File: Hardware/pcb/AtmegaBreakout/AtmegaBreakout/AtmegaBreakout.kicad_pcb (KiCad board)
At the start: 4 copper layers, 69.9 x 53.3 mm, 33 parts, among them J1 ANALOG, J2 POWER and COMMS, J3 DIGITAL1, J4 DIGITAL2, J5 DIGITAL3, J6 USB_B_Micro, SW1 EVP-ASAC1A, U1 ATMEGA2560-16AU, U2 CP2102N-A01-GQFN24, Y1 16MHz Ceramic Resonator

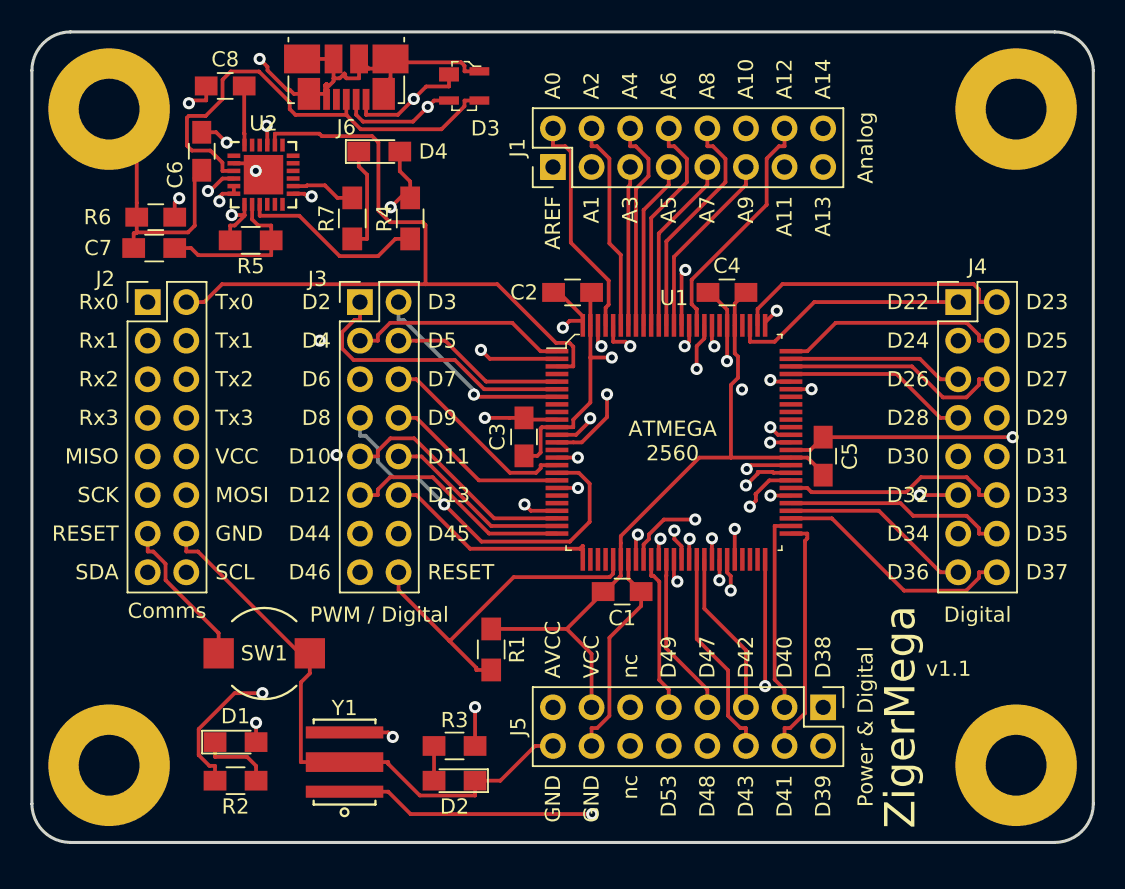
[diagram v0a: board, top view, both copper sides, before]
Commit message: Groundplane, Missing GND and VCC connection
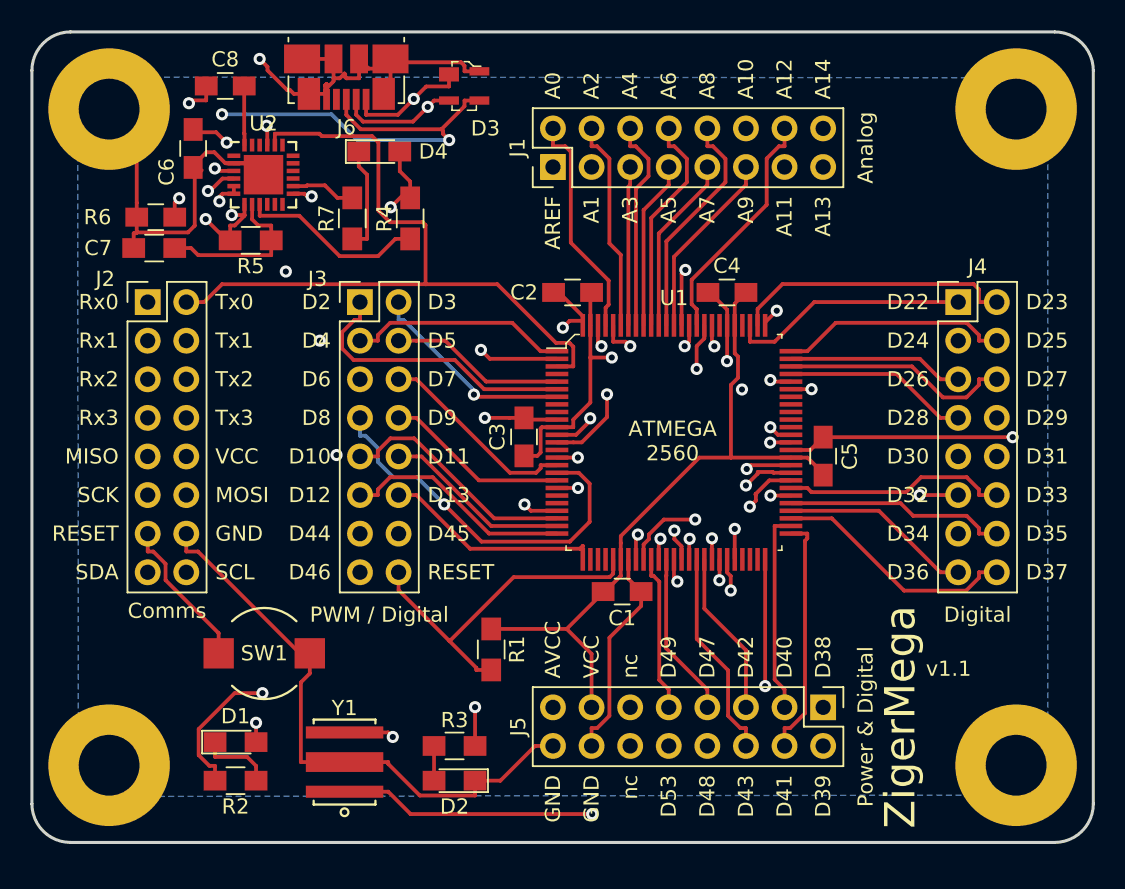
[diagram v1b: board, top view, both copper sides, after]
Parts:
- moved C6 0.60 mm to (83.0, 63.5)
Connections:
- D3 pad 1: Net-(D3-Pad1) -> GND
- D3 pad 2: /VBUS -> VCC
- J6 pad 1: /VBUS -> VCC
- J6 pad 5: Net-(D3-Pad1) -> GND
- J6 pad 6: Net-(D3-Pad1) -> GND
- R5 pad 2: /VBUS -> VCC
- U2 pad 2: Net-(D3-Pad1) -> GND
- U2 pad 25: Net-(D3-Pad1) -> GND
- U2 pad 7: /VBUS -> VCC
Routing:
- net VCC: track 96.8 -> 146.1 mm, vias 2 -> 6
- net GND: track 262.6 -> 308.4 mm, vias 3 -> 4
- net Net-(D3-Pad1): track 39.5 -> 0.00 mm, vias 2 -> 0
- net /VBUS: track 27.0 -> 0.00 mm, vias 2 -> 0
- net Net-(D3-Pad4): track 31.0 -> 32.8 mm, vias 0 -> 3
- added copper zone on B.Cu, net GND
